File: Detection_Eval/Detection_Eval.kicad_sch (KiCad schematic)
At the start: 18 parts, among them SW1 SW_Push, SW2 SW_Push, U1 74AHC1G08

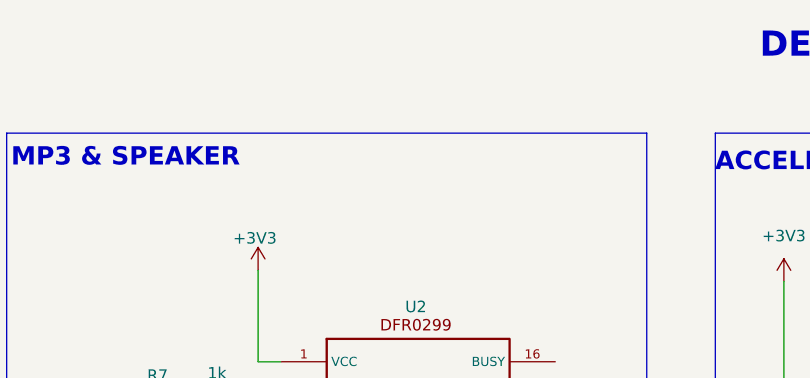
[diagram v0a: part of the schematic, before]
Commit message: Madison_02-05
1.2V to 5V battery regulator added
chose AAAA 600maH rechargeable battery
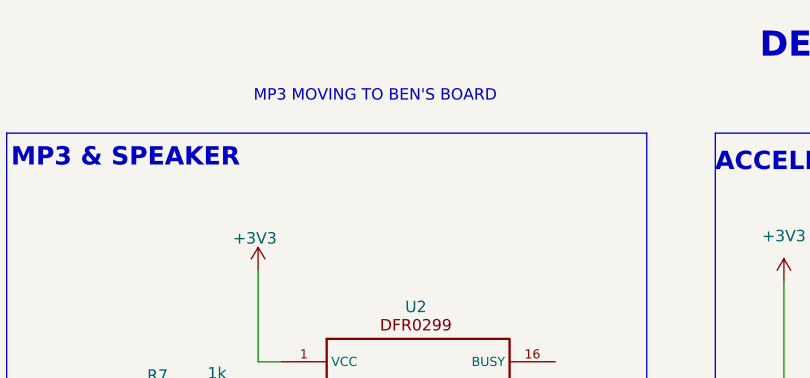
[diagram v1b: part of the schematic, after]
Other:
- note added: "MP3 MOVING TO BEN'S BOARD"
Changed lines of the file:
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@@
+		)
+	)
+	(text "MP3 MOVING TO BEN'S BOARD"
+		(exclude_from_sim no)
+		(at 51.562 26.416 0)
+		(effects
+			(font
+				(size 1.27 1.27)
+			)
+			(justify left)
 		)
 	)

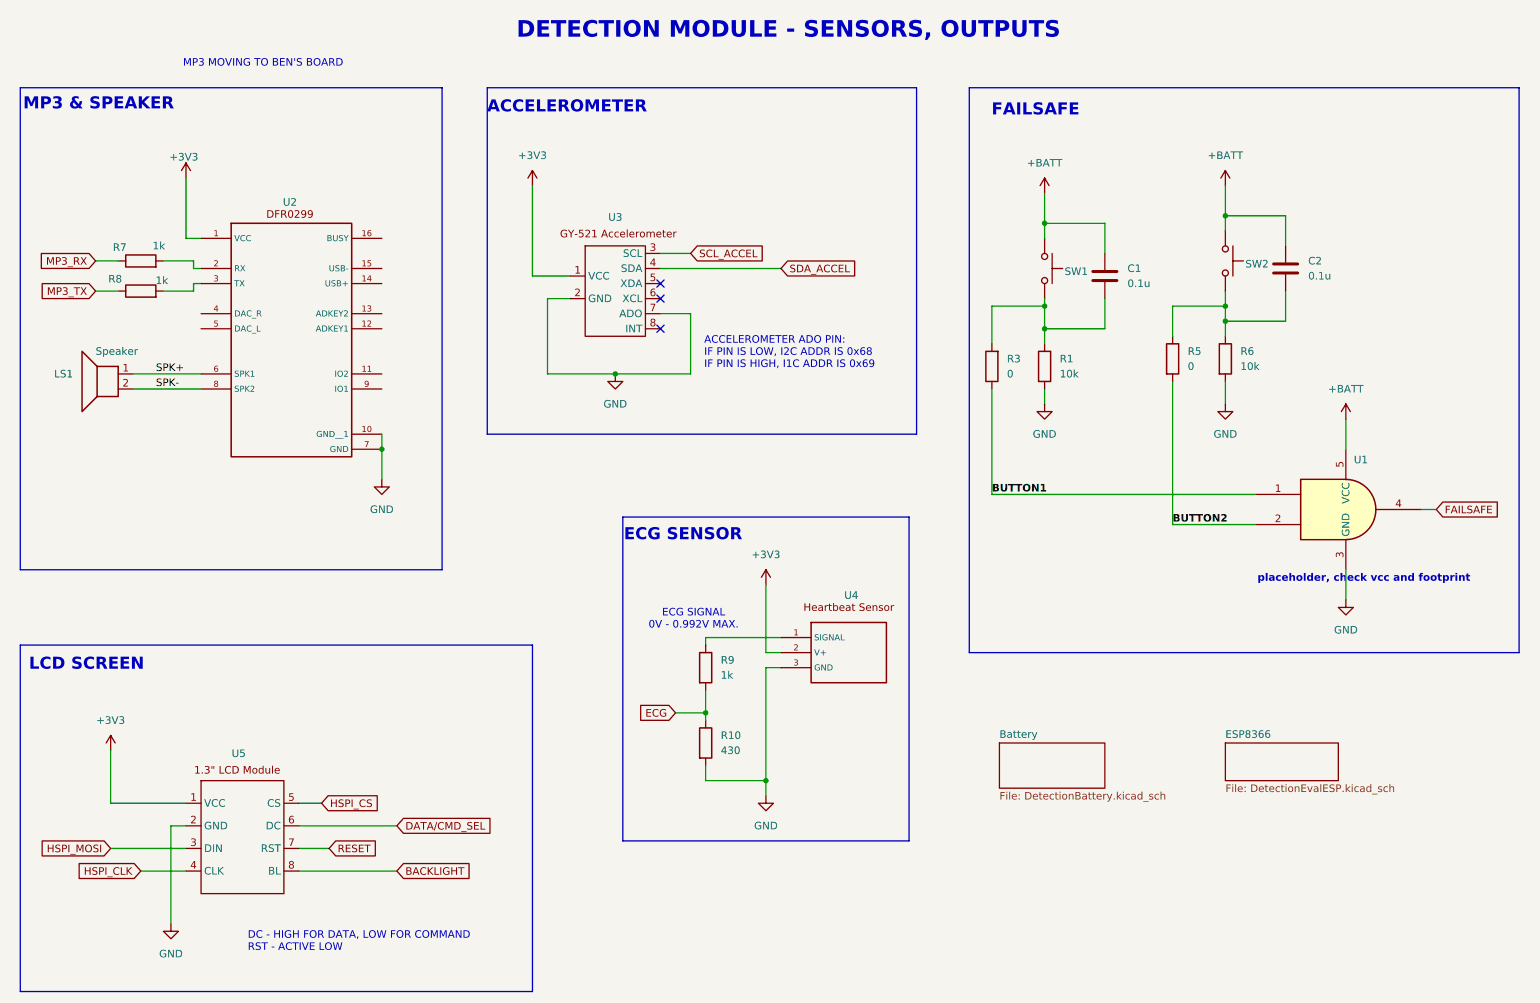
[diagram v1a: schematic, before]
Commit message: Madison_02-05_2
Added battery charger circuit
Added footprints to accelerometer, lcd screen, buttons, AND gate, batt charger, batt holder
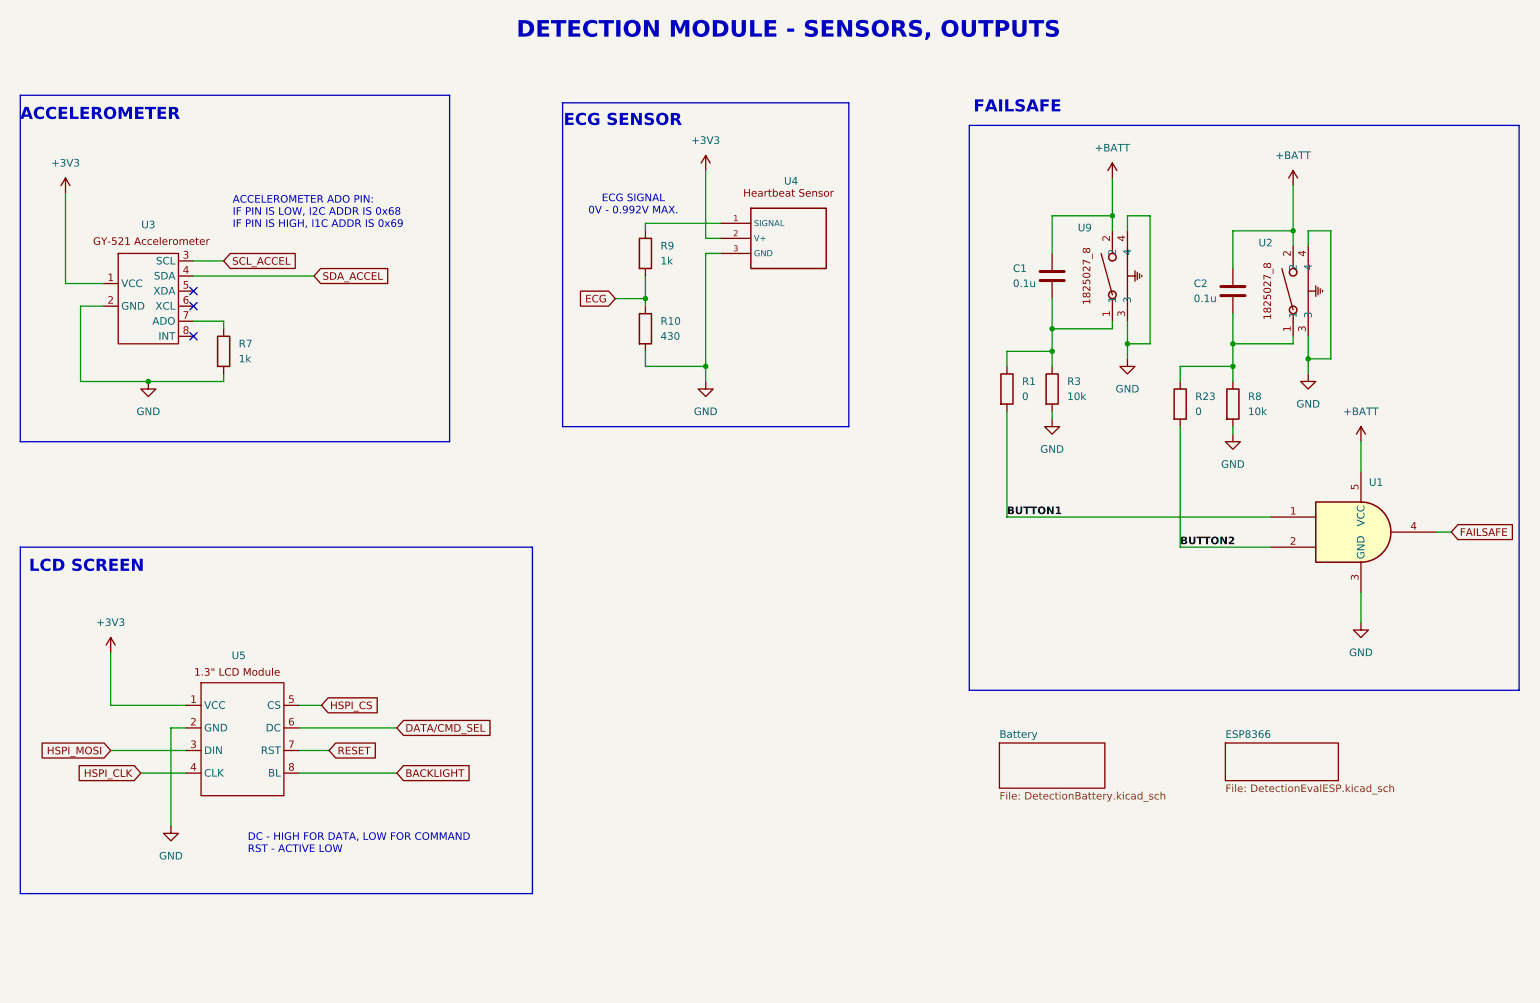
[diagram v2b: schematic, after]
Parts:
- removed LS1: Speaker, symbol Device:Speaker
- removed R5: 0, Resistor_SMD:R_0402_1005Metric, symbol Device:R
- removed R6: 10k, Resistor_SMD:R_0402_1005Metric, symbol Device:R
- removed SW1, SW2: SW_Push, symbol Switch:SW_Push
- removed U2: ~, symbol Detection_Eval_lib:DFR0299
- added R23: 0, Resistor_SMD:R_0402_1005Metric, symbol Device:R
- added U2, U9: ~, Detection_Eval_lib_fp:SW2_1825027-C_TEC, symbol Detection_Eval_lib:1825027_8BUTTON
- R1: value 10k -> 0
- R3: value 0 -> 10k
- R8: value 1k -> 10k
- U1: value 74AHC1G08 -> SN74LVC1G08DCKR; footprint (none) -> Package_TO_SOT_SMD:SOT-353_SC-70-5_Handsoldering
- U3: footprint (none) -> Detection_Eval_lib_fp:GY-521
- U5: footprint (none) -> Connector_PinHeader_2.54mm:PinHeader_1x08_P2.54mm_Vertical
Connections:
- net MP3_TX is gone; now on an unnamed net: R8.1
- net +BATT: now also U2.2, U9.2
- net BUTTON1: now also R1.2; no longer R3.1
- net BUTTON2: now also R23.2
- net GND: now also R3.2, R7.2, R8.2, U2.3, U2.4, U9.3, U9.4; no longer R1.2, U3.7 (ADO)
- net at C1.2, R1.1: now also R3.1, U9.1; no longer R3.2
- net at C2.2: now also R23.1, U2.1
- net MP3_RX: no longer names the net of R7.1
- net MP3_RX: now also U3.7 (ADO)
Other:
- note removed: "MP3 & SPEAKER"
- note removed: "MP3 MOVING TO BEN'S BOARD"
- note removed: "placeholder, check vcc and footprint"
- moved on the sheet: C2, R10, R9, U1, U3, U4, U5

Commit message: Madison_02-06
final footprints added and layout positioning mostly done
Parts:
- C1, C2: footprint (none) -> Capacitor_SMD:C_0603_1608Metric
- U5: footprint Connector_PinHeader_2.54mm:PinHeader_1x08_P2.54mm_Vertical -> Detection_Eval_lib_fp:LCDSCREEN
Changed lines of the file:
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@@
 			)
 		)
-		(property "Footprint" "Connector_PinHeader_2.54mm:PinHeader_1x08_P2.54mm_Vertical"
+		(property "Footprint" "Detection_Eval_lib_fp:LCDSCREEN"
 			(at 54.61 149.86 0)
 			(effects
@@
 			)
 		)
-		(property "Footprint" ""
+		(property "Footprint" "Capacitor_SMD:C_0603_1608Metric"
 			(at 229.5652 68.58 0)
 			(effects
@@
 			)
 		)
-		(property "Footprint" ""
+		(property "Footprint" "Capacitor_SMD:C_0603_1608Metric"
 			(at 199.0852 66.04 0)
 			(effects

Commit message: LAYOUT DONE
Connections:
- net +BATT renamed +5V
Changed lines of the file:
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@@
 			)
 		)
-		(property "Value" "+BATT"
+		(property "Value" "+5V"
 			(at 238.76 41.91 0)
 			(effects
@@
 			)
 		)
-		(property "Value" "+BATT"
+		(property "Value" "+5V"
 			(at 250.19 85.09 0)
 			(effects
@@
 			)
 		)
-		(property "Value" "+BATT"
+		(property "Value" "+5V"
 			(at 208.28 40.64 0)
 			(effects
